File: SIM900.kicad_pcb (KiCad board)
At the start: 2 copper layers, 65 parts, among them J1 Conn_01x05, J10 Conn_01x02, J11 Conn_Coaxial_Power, J12 AudioJack2_Ground, J13 AudioJack2_Ground, J2 Conn_01x07, J3 Conn_01x04, J4 Conn_01x06, J5 Conn_01x02, J6 Conn_01x06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

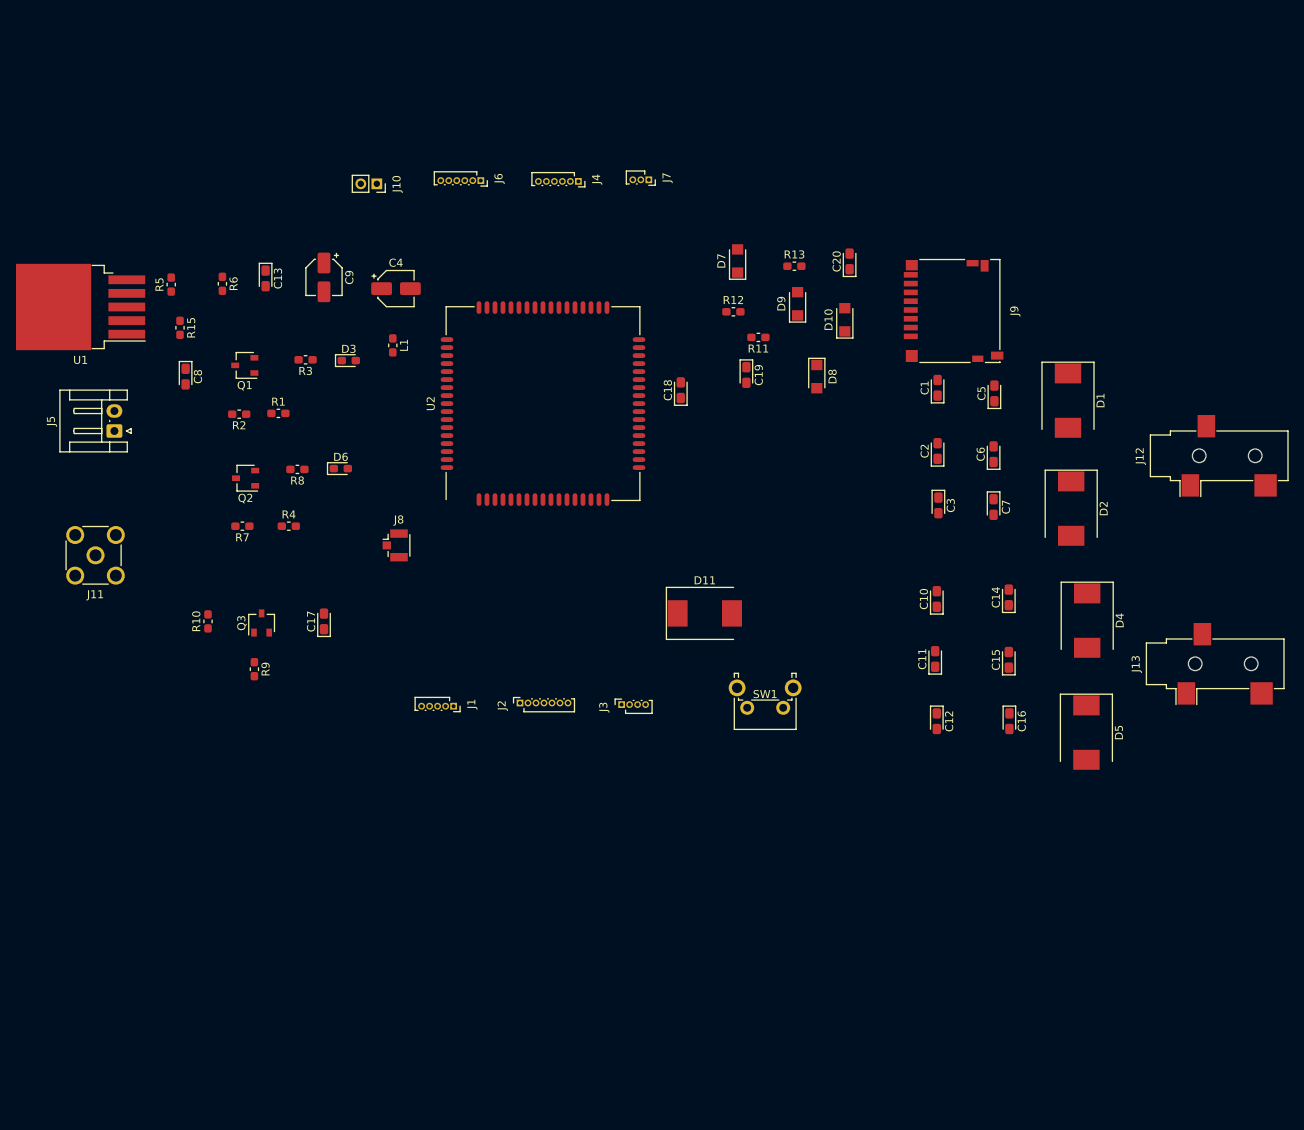
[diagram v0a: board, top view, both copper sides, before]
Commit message: Se incluyo el poncho de la EDU CIAA y se ordenaron los componentes dentro de ella
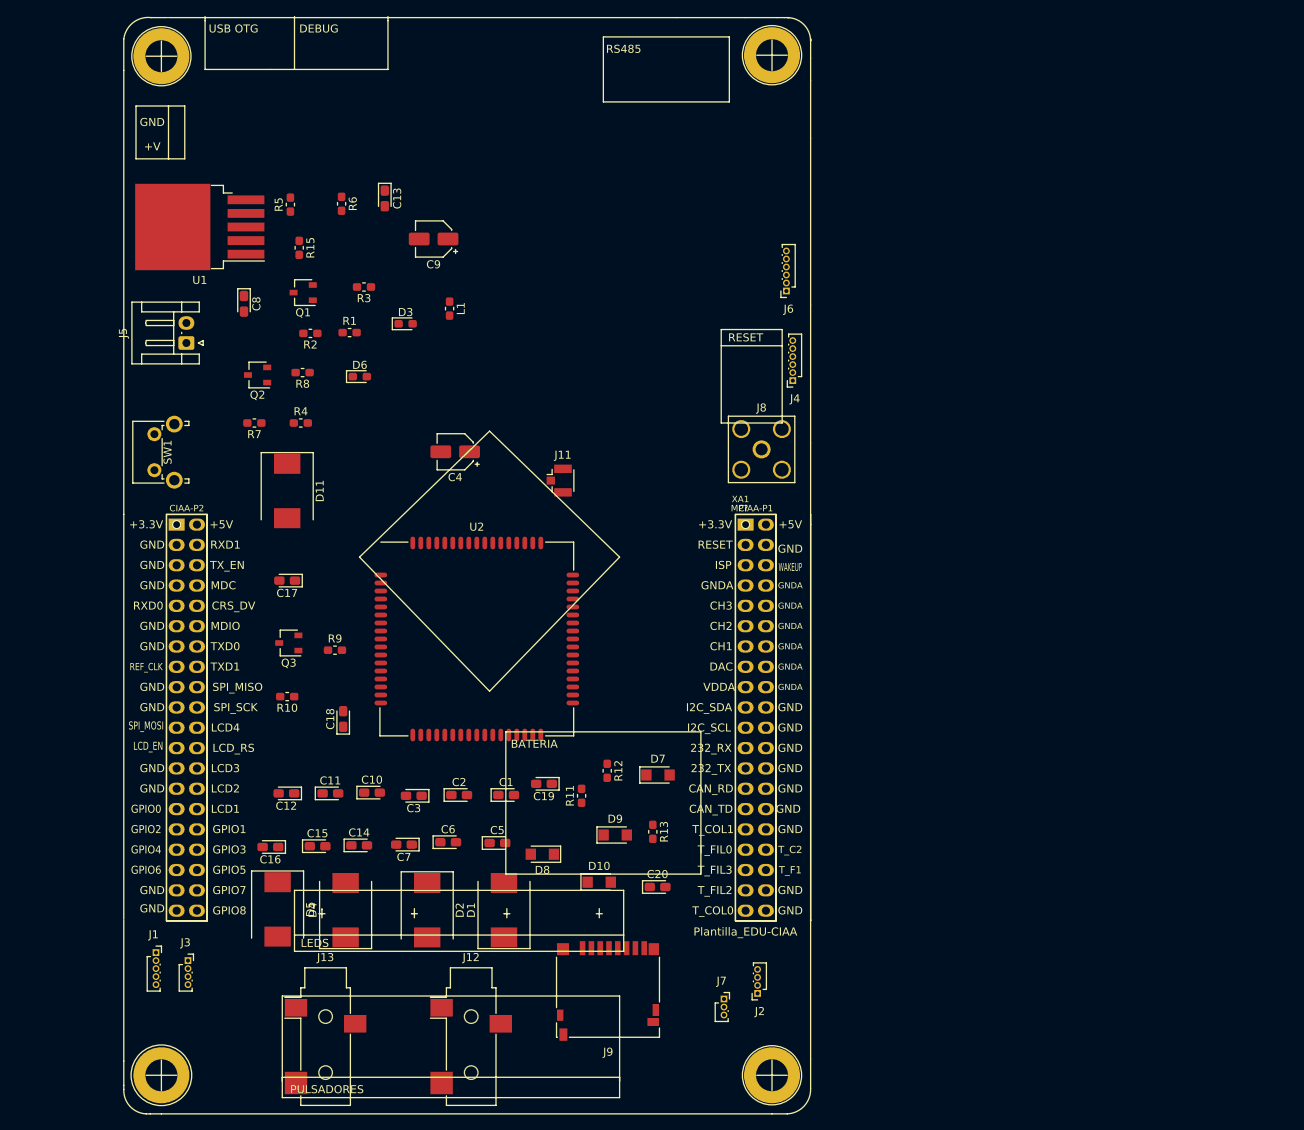
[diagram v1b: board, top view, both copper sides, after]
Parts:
- removed J10: Conn_01x02, Connector_PinSocket_2.00mm:PinSocket_1x02_P2.00mm_Vertical
- added MP?: Plantilla_EDU-CIAA, Poncho_Esqueleto:Plantilla_EDU-CIAA, F.Cu at (150.8, 98.3)
- added XA1: Conn_Poncho2P_2x_20x2, Poncho_Esqueleto:Conn_Poncho_Completo, F.Cu at (150.8, 98.3)
- J11: footprint Connector_Coaxial:SMA_Molex_73251-2200_Horizontal -> Connector_Coaxial:U.FL_Hirose_U.FL-R-SMT-1_Vertical
- J2: value Conn_01x07 -> Conn_01x04; footprint Connector_PinSocket_1.00mm:PinSocket_1x07_P1.00mm_Vertical -> Connector_PinSocket_1.00mm:PinSocket_1x04_P1.00mm_Vertical
- J8: footprint Connector_Coaxial:U.FL_Hirose_U.FL-R-SMT-1_Vertical -> Connector_Coaxial:SMA_Amphenol_132203-12_Horizontal
- moved J13 120.6 mm to (98.3, 162.3), turned to 0 degrees
- moved J12 118.4 mm to (116.5, 162.3), turned to 0 degrees
- moved D5 103.5 mm to (92.3, 146.4)
- moved J7 102.8 mm to (148.1, 157.6), turned to 0 degrees
- moved D4 99.5 mm to (100.8, 146.5), turned to 90 degrees
- moved J9 95.3 mm to (133.6, 156.6), turned to 180 degrees
- moved D1 95.0 mm to (120.6, 146.5), turned to 90 degrees
- moved D2 94.9 mm to (111.0, 146.5)
- moved C16 93.7 mm to (91.4, 138.6), turned to 180 degrees
- moved C15 89.5 mm to (97.3, 138.5), turned to 0 degrees
- moved C14 86.9 mm to (102.5, 138.4), turned to 0 degrees
- moved C7 84.9 mm to (108.1, 138.3), turned to 180 degrees
- moved SW1 84.0 mm to (76.9, 91.5), turned to 90 degrees
- moved C5 83.8 mm to (119.8, 138.1), turned to 0 degrees
- moved C6 83.7 mm to (113.6, 138.0), turned to 0 degrees
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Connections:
- net Net-(C4-Pad1) renamed /VCD_5V
- U2 pad 10: Net-(J2-Pad7) -> /RXD
- U2 pad 27: Net-(J1-Pad1) -> Net-(J2-Pad1)
- U2 pad 28: Net-(J1-Pad2) -> Net-(J2-Pad2)
- U2 pad 3: Net-(J2-Pad1) -> Net-(J1-Pad1)
- U2 pad 37: Net-(J1-Pad3) -> Net-(J2-Pad3)
- U2 pad 38: Net-(J1-Pad4) -> Net-(J2-Pad4)
- U2 pad 4: Net-(J2-Pad2) -> Net-(J1-Pad2)
- U2 pad 5: Net-(J2-Pad3) -> Net-(J1-Pad3)
- U2 pad 7: Net-(J2-Pad4) -> Net-(J1-Pad4)
- U2 pad 8: Net-(J2-Pad5) -> Net-(J1-Pad5)
- U2 pad 9: Net-(J2-Pad6) -> /TXD

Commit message: Se ordeno mejor los componentes y se redujo la planilla de la EDU CIAA
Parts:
- added FID1: Fiducial, Fiducial:Fiducial_0.75mm_Mask2.25mm, F.Cu at (131.0, 42.0)
- added H1: MountingHole, MountingHole:MountingHole_2.5mm_Pad, F.Cu at (63.0, 43.0)
- added H2: MountingHole, MountingHole:MountingHole_2.5mm_Pad, F.Cu at (131.0, 50.0)
- added H3: MountingHole, MountingHole:MountingHole_2.5mm_Pad, F.Cu at (131.0, 160.0)
- added H4: MountingHole, MountingHole:MountingHole_2.5mm_Pad, F.Cu at (55.0, 160.0)
- D1, D11, D2, D4, D5: footprint Diode_SMD:D_SMC -> Diode_SMD:D_SMA_Handsoldering
- D3, D6: footprint LED_SMD:LED_0603_1608Metric_Pad1.05x0.95mm_HandSolder -> LED_SMD:LED_0805_2012Metric
- J1: footprint Connector_PinSocket_1.00mm:PinSocket_1x05_P1.00mm_Vertical -> Connector_PinHeader_2.00mm:PinHeader_1x05_P2.00mm_Vertical
- J2, J3: footprint Connector_PinSocket_1.00mm:PinSocket_1x04_P1.00mm_Vertical -> Connector_PinHeader_2.00mm:PinHeader_1x04_P2.00mm_Vertical
- J4, J6: footprint Connector_PinSocket_1.00mm:PinSocket_1x06_P1.00mm_Vertical -> Connector_PinHeader_2.00mm:PinHeader_1x06_P2.00mm_Vertical
- J7: footprint Connector_PinSocket_1.00mm:PinSocket_1x03_P1.00mm_Vertical -> Connector_PinHeader_2.00mm:PinHeader_1x03_P2.00mm_Vertical
- R1, R10, R11, R12, R13, R15, R2, R3, R4, R5, R6, R7, R8, R9: footprint Resistor_SMD:R_0603_1608Metric_Pad1.05x0.95mm_HandSolder -> Resistor_SMD:R_0805_2012Metric_Pad1.15x1.40mm_HandSolder
- XA1: footprint Poncho_Esqueleto:Conn_Poncho_Completo -> Poncho_Esqueleto:Conn_Poncho_Chico
- moved MP? 172.2 mm to (-21.0, 110.0)
- moved J1 101.0 mm to (56.0, 53.0)
- moved J7 92.1 mm to (57.0, 144.0)
- moved J3 90.4 mm to (56.0, 66.0)
- moved Q1 41.2 mm to (112.0, 107.0), turned to 270 degrees
- moved R2 39.2 mm to (118.0, 107.1), turned to 270 degrees
- moved R3 32.5 mm to (111.0, 100.1), turned to 270 degrees
- moved R1 31.2 mm to (118.0, 100.7), turned to 90 degrees
- moved J5 29.9 mm to (77.0, 46.0), turned to 0 degrees
- moved D11 29.3 mm to (67.0, 81.5)
- moved C4 29.2 mm to (89.0, 75.0), turned to 0 degrees
- moved C18 29.0 mm to (76.0, 107.0)
- moved L1 28.5 mm to (87.0, 81.0)
- moved J6 27.9 mm to (128.0, 70.0)
- moved J4 27.7 mm to (131.0, 70.0)
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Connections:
- J1 pad 5: /RST_EXT -> Net-(J1-Pad5)
- XA1 pad 1: +3V3 -> Net-(XA1-Pad1)
- XA1 pad 2: /VCD_5V -> +5V
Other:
- board outline added: 86 x 127 mm
- copper layers 2 -> 4

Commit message: Se completo el PCB y se corrigieron la mayoria de las observaciones del profeor
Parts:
- added FID2: Fiducial, Fiducial:Fiducial_0.75mm_Mask2.25mm, F.Cu at (54.0, 43.0)
- added FID3: Fiducial, Fiducial:Fiducial_0.75mm_Mask2.25mm, F.Cu at (55.0, 153.0)
- C1, C10, C11, C12, C13, C14, C15, C16, C17, C18, C19, C2, C20, C3, C5, C6, C7, C8: footprint Capacitor_Tantalum_SMD:CP_EIA-2012-12_Kemet-R_Pad1.30x1.05mm_HandSolder -> Capacitor_SMD:C_0805_2012Metric
- C4, C9: footprint Capacitor_SMD:CP_Elec_4x3 -> Capacitor_SMD:C_0805_2012Metric
- moved MP? 24.3 mm to (-25.0, 86.0)
- moved D11 24.1 mm to (65.0, 57.5)
- moved SW1 24.1 mm to (52.0, 59.0)
- moved D3 12.5 mm to (114.5, 82.1)
- moved R3 12.5 mm to (114.5, 88.1)
- moved J1 12.0 mm to (57.0, 65.0)
- moved J3 12.0 mm to (57.0, 78.0)
- moved J6 12.0 mm to (127.0, 58.0)
- moved R1 12.0 mm to (119.0, 88.7)
- moved R2 12.0 mm to (119.0, 95.1)
- moved Q1 11.9 mm to (113.5, 95.2)
- moved R9 11.0 mm to (76.0, 111.0)
- moved R4 10.4 mm to (71.0, 65.0)
- moved D6 10.2 mm to (78.0, 70.9)
- moved Q2 10.2 mm to (77.4, 58.8)
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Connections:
- net /ANT renamed Net-(J11-Pad1)
- net /MIC_N renamed Net-(C11-Pad1)
- net /MIC_P renamed Net-(C10-Pad1)
- C1 pad 1: /SPK_P -> Net-(C1-Pad1)
- C2 pad 1: /SPK_N -> Net-(C2-Pad1)
- C2 pad 2: /SPK_P -> Net-(C1-Pad1)
- C3 pad 1: /SPK_N -> Net-(C2-Pad1)
- C4 pad 1: /VCD_5V -> +5V
- C5 pad 1: /SPK_P -> Net-(C1-Pad1)
- C6 pad 1: /SPK_N -> Net-(C2-Pad1)
- C6 pad 2: /SPK_P -> Net-(C1-Pad1)
- C7 pad 1: /SPK_N -> Net-(C2-Pad1)
- C8 pad 1: /VCD_5V -> +5V
- D1 pad 2: /SPK_P -> Net-(C1-Pad1)
- D2 pad 1: /SPK_N -> Net-(C2-Pad1)
- D3 pad 2: /VBAT -> +3V3
- D6 pad 2: /VBAT -> +3V3
- J12 pad S: /SPK_N -> Net-(C1-Pad1)
- J12 pad T: /SPK_P -> Net-(C2-Pad1)
- L1 pad 2: /VBAT -> +3V3
- R15 pad 1: /VCD_5V -> +5V
- U1 pad 2: /VCD_5V -> +5V
- U2 pad 21: /SPK_P -> Net-(C1-Pad1)
- U2 pad 22: /SPK_N -> Net-(C2-Pad1)
- U2 pad 55: /VBAT -> +3V3
- U2 pad 56: /VBAT -> +3V3
- U2 pad 57: /VBAT -> +3V3
- XA1 pad 2: +5V -> Net-(XA1-Pad2)
- XA1 pad 41: +3V3 -> Net-(XA1-Pad41)
- XA1 pad 42: /VCD_5V -> +5V
- XA1 pad 69: /RST_EXT -> Net-(XA1-Pad69)
- XA1 pad 72: Net-(XA1-Pad72) -> /RST_EXT
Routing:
- net GND: track 0.00 -> 735.0 mm, vias 0 -> 39
- net Net-(J7-Pad2): track 0.00 -> 96.5 mm, vias 0 -> 2
- net Net-(J7-Pad3): track 0.00 -> 96.4 mm, vias 0 -> 2
- net Net-(C11-Pad1): track 0.00 -> 77.7 mm, vias 0 -> 2
- net Net-(J7-Pad1): track 0.00 -> 74.3 mm, vias 0 -> 2
- net Net-(C10-Pad1): track 0.00 -> 72.7 mm
- net Net-(J5-Pad1): track 0.00 -> 72.1 mm, vias 0 -> 2
- net Net-(C1-Pad1): track 0.00 -> 70.4 mm, vias 0 -> 2
- net +5V: track 0.00 -> 67.2 mm, vias 0 -> 4
- net Net-(J2-Pad1): track 0.00 -> 66.8 mm, vias 0 -> 2
- net Net-(J2-Pad2): track 0.00 -> 64.9 mm, vias 0 -> 2
- net Net-(C2-Pad1): track 0.00 -> 63.8 mm
- net Net-(J2-Pad3): track 0.00 -> 62.5 mm, vias 0 -> 2
- net Net-(J2-Pad4): track 0.00 -> 62.2 mm, vias 0 -> 2
- net /RXD: track 0.00 -> 61.4 mm, vias 0 -> 2
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- added copper zone on B.Cu, net (none)
- added copper zone on F.Cu, net (none)
- added copper zone on In1.Cu_VCD, net +3V3
- added copper zone on In2.Cu_GND, net GND
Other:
- board size 86 x 127 mm -> 88 x 127 mm
- net class Default: clearance 0.2 -> 0.25
- rule trace_clearance: 0.2 -> 0.25

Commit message: Se mejoro el conexionado en el PCB
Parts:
- removed MP?: Plantilla_EDU-CIAA, Poncho_Esqueleto:Plantilla_EDU-CIAA
- moved C18 8.14 mm to (93.1, 106.5)
- moved C17 5.70 mm to (75.9, 98.7)
- moved J4 4.07 mm to (131.1, 72.3)
- moved J6 4.07 mm to (131.1, 58.3)
- moved J2 2.81 mm to (130.8, 150.1)
- moved J1 2.26 mm to (56.8, 67.2)
- moved J3 2.16 mm to (56.7, 80.1)
- moved J8 2.02 mm to (131.6, 80.3)
- moved R15 1.00 mm to (88.0, 60.0)
- moved R5 1.00 mm to (94.0, 60.0)
- moved R6 1.00 mm to (100.0, 60.0)
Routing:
- net GND: track 735.0 -> 169.5 mm, vias 39 -> 37
- net +3V3: track 52.4 -> 21.0 mm
- net Net-(C18-Pad1): track 22.2 -> 6.01 mm, vias 2 -> 0
- net Net-(J6-Pad5): track 57.9 -> 72.5 mm
- net /RXD: track 61.4 -> 47.7 mm
- net Net-(J6-Pad6): track 61.1 -> 73.1 mm
- net +5V: track 67.2 -> 77.5 mm
- net Net-(J2-Pad3): track 62.5 -> 70.7 mm
- net Net-(J2-Pad4): track 62.2 -> 68.8 mm
- net /TXD: track 61.3 -> 66.9 mm
- net Net-(J5-Pad1): track 72.1 -> 67.3 mm, vias 2 -> 4
- net Net-(J7-Pad3): track 96.4 -> 100.8 mm
- net /CLK: track 25.5 -> 21.2 mm
- net /STATUS: track 28.1 -> 24.2 mm, vias 0 -> 2
- net Net-(J6-Pad4): track 41.7 -> 45.5 mm
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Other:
- net class Default: clearance 0.25 -> 0.3
- rule trace_clearance: 0.25 -> 0.3

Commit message: Se realizaron los cambios a los comentarios hechos por el profesor
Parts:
- L1: footprint Inductor_SMD:L_0603_1608Metric_Pad1.05x0.95mm_HandSolder -> Inductor_SMD:L_0805_2012Metric
- moved J8 28.1 mm to (130.7, 52.2)
- moved D3 13.9 mm to (114.8, 96.0)
- moved J6 13.1 mm to (130.4, 71.3)
- moved J4 13.1 mm to (130.4, 85.3)
- moved R3 12.8 mm to (113.0, 100.8)
- moved Q1 11.5 mm to (114.0, 106.7)
- moved R2 7.01 mm to (119.6, 102.1)
- moved R1 6.84 mm to (119.6, 95.5)
- moved J11 3.63 mm to (109.2, 68.3), turned to 90 degrees
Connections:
- U2 pad 10: /RXD -> /TXD
- U2 pad 9: /TXD -> /RXD
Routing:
- net +3V3: track 21.0 -> 63.7 mm
- net /RXD: track 47.7 -> 73.0 mm
- net Net-(J4-Pad2): track 43.8 -> 27.2 mm, vias 2 -> 0
- net Net-(J4-Pad6): track 44.2 -> 28.0 mm, vias 2 -> 0
- net Net-(J4-Pad3): track 43.1 -> 27.6 mm, vias 2 -> 0
- net Net-(J6-Pad1): track 44.7 -> 29.3 mm, vias 2 -> 0
- net Net-(J4-Pad5): track 43.2 -> 28.4 mm, vias 2 -> 0
- net Net-(J6-Pad2): track 44.3 -> 29.7 mm, vias 2 -> 0
- net Net-(J6-Pad3): track 44.5 -> 30.1 mm, vias 2 -> 0
- net Net-(J6-Pad4): track 45.5 -> 31.2 mm, vias 2 -> 0
- net Net-(J4-Pad4): track 42.3 -> 28.0 mm, vias 2 -> 0
- net Net-(J6-Pad6): track 73.1 -> 59.4 mm, vias 2 -> 0
- net Net-(J4-Pad1): track 40.2 -> 26.8 mm, vias 2 -> 0
- net /NETLIGHT: track 26.0 -> 37.1 mm, vias 0 -> 2
- net Net-(J6-Pad5): track 72.5 -> 61.7 mm
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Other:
- board text added: "NOTA: TRACK: 0,8 mm Y 0,7 mm VIA: 1,6 mm/0,8 mm CLEARENCE: 0,3 mm GRID: 1 mm FABRICANTE: Seeed Technology Co., Ltd"
- board text added: "SIM900 KICAD FREDS AMUNDARAY"
